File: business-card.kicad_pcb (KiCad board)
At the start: 2 copper layers, 0 parts

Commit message: Placed the CH logo in schematic and pcb
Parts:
- added LOGO1: CH_Logo, business-card:CH_Logo_20mm_SilkScreen, F.Cu at (198.5, 120.7)
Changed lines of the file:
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@@
 		)
+	)
+	(footprint "business-card:CH_Logo_20mm_SilkScreen"
+		(layer "F.Cu")
+		(at 198.5 120.741935)
+		(descr "CH monogram from ch-logo-option-01.svg; 20 mm artwork width, 15.483871 mm height; filled front silkscreen")
+		(tags "CH monogram logo silkscreen")
+		(property "Reference" "LOGO1"
+			(at 0 -9.241935 0)
+			(layer "F.SilkS")
+			(hide yes)
+			(effects
+				(font
+					(size 1 1)
+					(thickness 0.15)
+				)
+			)
+		)
+		(property "Value" "CH_Logo"
+			(at 0 9.241935 0)
+			(layer "F.Fab")
+			(hide yes)
+			(effects
+				(font
+					(size 1 1)
+					(thickness 0.15)
+				)
+			)
+		)
+		(property "Datasheet" ""
+			(at 0 0 0)
+			(layer "F.Fab")
+			(hide yes)
+			(effects
+				(font
+					(size 1.27 1.27)
+				)
+			)
+		)
+		(property "Description" "CH monogram with a 20 mm wide front-silkscreen footprint; no electrical pins"
+			(at 0 0 0)
+			(layer "F.Fab")
+			(hide yes)
+			(effects
+				(font
+					(size 1.27 1.27)
+				)
+			)
+		)
+		(property ki_fp_filters "CH_Logo_*_SilkScreen")
+		(sheetname "/")
+		(sheetfile "business-card.kicad_sch")
+		(units
+			(unit
+				(name "A")
+				(pins)
+			)
+		)
+		(attr exclude_from_pos_files exclude_from_bom allow_missing_courtyard)
+		(duplicate_pad_numbers_are_jumpers no)
+		(fp_poly
+			(pts
+				(xy 0.799439 -7.741935) (xy 0.827489 -7.73913) (xy 0.85554 -7.730715) (xy 0.88359 -7.71669) (xy 0.911641 -7.697055)
+				(xy 3.520337 -5.587658) (xy 3.544881 -5.562412) (xy 3.562412 -5.534362) (xy 3.572931 -5.503506)
+				(xy 3.576438 -5.469846) (xy 3.576438 -0.897616) (xy 7.279102 -0.897616) (xy 7.279102 -4.670407)
+				(xy 7.28068 -4.698852) (xy 7.285414 -4.721073) (xy 7.293303 -4.73707) (xy 7.304348 -4.746844) (xy 7.318548 -4.750394)
+				(xy 7.335905 -4.747721) (xy 7.356417 -4.738824) (xy 7.380084 -4.723703) (xy 9.943899 -2.86115) (xy 9.968443 -2.838359)
+				(xy 9.985975 -2.812062) (xy 9.996494 -2.782258) (xy 10 -2.748948) (xy 10 5.441795) (xy 9.996494 5.475105)
+				(xy 9.985975 5.504909) (xy 9.968443 5.531206) (xy 9.943899 5.553997) (xy 7.380084 7.495091) (xy 7.356417 7.51087)
+				(xy 7.335905 7.520337) (xy 7.318548 7.523492) (xy 7.304348 7.520337) (xy 7.293303 7.51087) (xy 7.285414 7.495091)
+				(xy 7.28068 7.473001) (xy 7.279102 7.4446) (xy 7.279102 1.12202) (xy 3.576438 1.12202) (xy 3.576438 5.497896)
+				(xy 3.572931 5.531381) (xy 3.562412 5.561711) (xy 3.544881 5.588885) (xy 3.520337 5.612903) (xy 0.841515 7.69425)
+				(xy 0.822833 7.708089) (xy 0.805356 7.719451) (xy 0.789084 7.728338) (xy 0.774018 7.734748) (xy 0.760157 7.738681)
+				(xy 0.747502 7.740138) (xy 0.736051 7.739119) (xy 0.725806 7.735624) (xy 0.716767 7.729652) (xy 0.708932 7.721204)
+				(xy 0.702303 7.71028) (xy 0.696879 7.696879) (xy 0.692661 7.681002) (xy 0.689648 7.662649) (xy 0.68784 7.641819)
+				(xy 0.687237 7.618513) (xy 0.687237 -7.629734) (xy 0.68899 -7.656031) (xy 0.69425 -7.678822) (xy 0.703015 -7.698107)
+				(xy 0.715288 -7.713885) (xy 0.731066 -7.726157) (xy 0.750351 -7.734923) (xy 0.773142 -7.740182)
+				(xy 0.799439 -7.741935)
+			)
+			(stroke
+				(width 0)
+				(type solid)
+			)
+			(fill yes)
+			(layer "F.SilkS")
+		)
+		(fp_poly
+			(pts
+				(xy -4.656381 -7.741935) (xy -0.771388 -7.741935) (xy -0.751665 -7.740621) (xy -0.734572 -7.736676)
+				(xy -0.720109 -7.730102) (xy -0.708275 -7.720898) (xy -0.699071 -7.709064) (xy -0.692496 -7.6946)
+				(xy -0.688552 -7.677507) (xy -0.687237 -7.657784) (xy -0.687237 -6.690042) (xy -0.688157 -6.672993)
+				(xy -0.690919 -6.656907) (xy -0.695521 -6.641786) (xy -0.701964 -6.62763) (xy -0.710247 -6.614437)
+				(xy -0.720372 -6.602209) (xy -0.732337 -6.590945) (xy -0.746143 -6.580645) (xy -7.023843 -2.31136)
+				(xy -7.037649 -2.301061) (xy -7.049614 -2.289797) (xy -7.059739 -2.277568) (xy -7.068022 -2.264376)
+				(xy -7.074465 -2.250219) (xy -7.079067 -2.235098) (xy -7.081829 -2.219013) (xy -7.082749 -2.201964)
+				(xy -7.082749 2.356241) (xy -7.081829 2.373291) (xy -7.079067 2.389376) (xy -7.074465 2.404497)
+				(xy -7.068022 2.418654) (xy -7.059739 2.431846) (xy -7.049614 2.444074) (xy -7.037649 2.455338)
+				(xy -7.023843 2.465638) (xy -0.746143 6.720898) (xy -0.732337 6.731197) (xy -0.720372 6.742461)
+				(xy -0.710247 6.75469) (xy -0.701964 6.767882) (xy -0.695521 6.782039) (xy -0.690919 6.79716) (xy -0.688157 6.813245)
+				(xy -0.687237 6.830295) (xy -0.687237 7.657784) (xy -0.688552 7.677507) (xy -0.692496 7.6946) (xy -0.699071 7.709064)
+				(xy -0.708275 7.720898) (xy -0.720109 7.730102) (xy -0.734572 7.736676) (xy -0.751665 7.740621)
+				(xy -0.771388 7.741935) (xy -4.57223 7.741935) (xy -4.606417 7.739481) (xy -4.63885 7.732118) (xy -4.66953 7.719846)
+				(xy -4.698457 7.702665) (xy -9.941094 3.98317) (xy -9.9549 3.972212) (xy -9.966865 3.960379) (xy -9.97699 3.947668)
+				(xy -9.985273 3.934081) (xy -9.991716 3.919618) (xy -9.996318 3.904278) (xy -9.99908 3.888061) (xy -10 3.870968)
+				(xy -10 -3.604488) (xy -9.996494 -3.637798) (xy -9.985975 -3.667602) (xy -9.968443 -3.693899) (xy -9.943899 -3.71669)
+				(xy -4.782609 -7.69986) (xy -4.753682 -7.718268) (xy -4.723001 -7.731417) (xy -4.690568 -7.739306)
+				(xy -4.656381 -7.741935)
+			)
+			(stroke
+				(width 0)
+				(type solid)
+			)
+			(fill yes)
+			(layer "F.SilkS")
+		)
+		(embedded_fonts no)
 	)
 	(embedded_fonts no)

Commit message: Add credit card board outline and getting started components
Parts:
- added BT1: 3V, Battery:BatteryHolder_Keystone_1058_1x2032, B.Cu at (128.5, 88.5)
- added D1: red, LED_THT:LED_D5.0mm, F.Cu at (143.0, 111.0)
- added R1: 1k, Resistor_THT:R_Axial_DIN0309_L9.0mm_D3.2mm_P12.70mm_Horizontal, F.Cu at (114.0, 98.5)
- moved LOGO1 29.3 mm to (170.5, 112.0)
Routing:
- net /led: track 0.00 -> 26.5 mm
- net GND: track 0.00 -> 22.8 mm, vias 0 -> 1
- net VCC: track 0.00 -> 10.8 mm, vias 0 -> 1
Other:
- board outline added: 85.6 x 54 mm

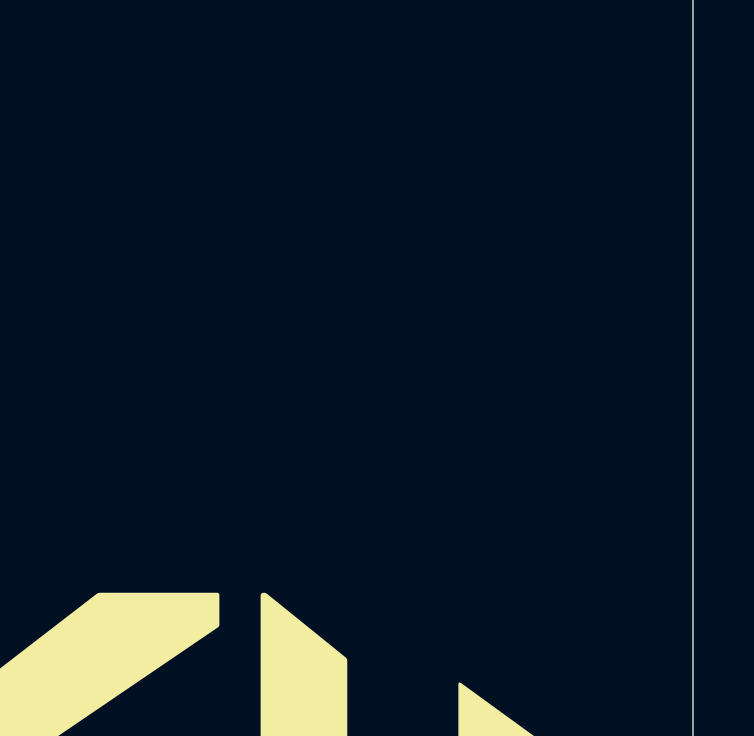
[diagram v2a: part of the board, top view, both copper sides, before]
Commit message: Place the contactless tap icon
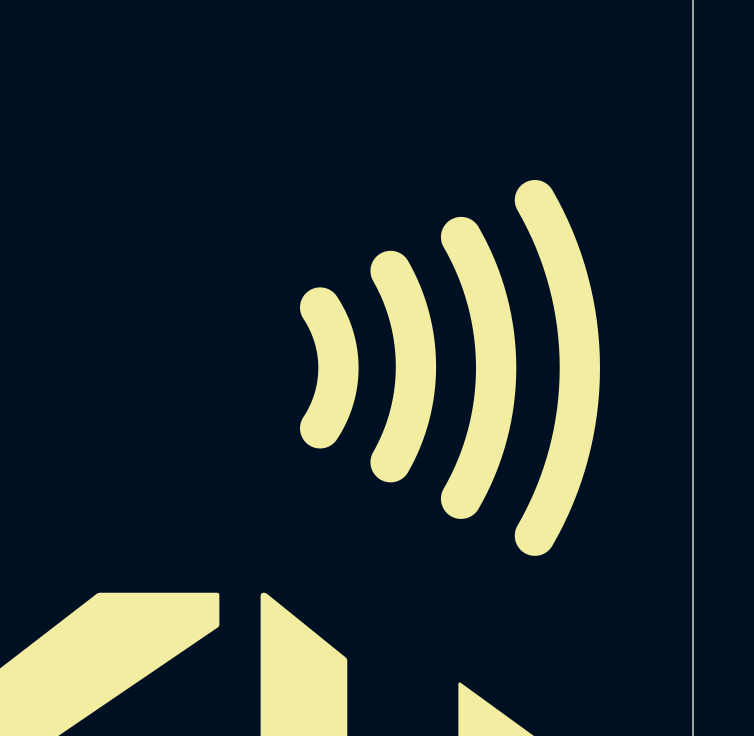
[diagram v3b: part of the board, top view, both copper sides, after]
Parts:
- added LOGO2: Contactless_Logo, business-card:Contactless_Logo_10mm_SilkScreen, F.Cu at (177.5, 96.8)

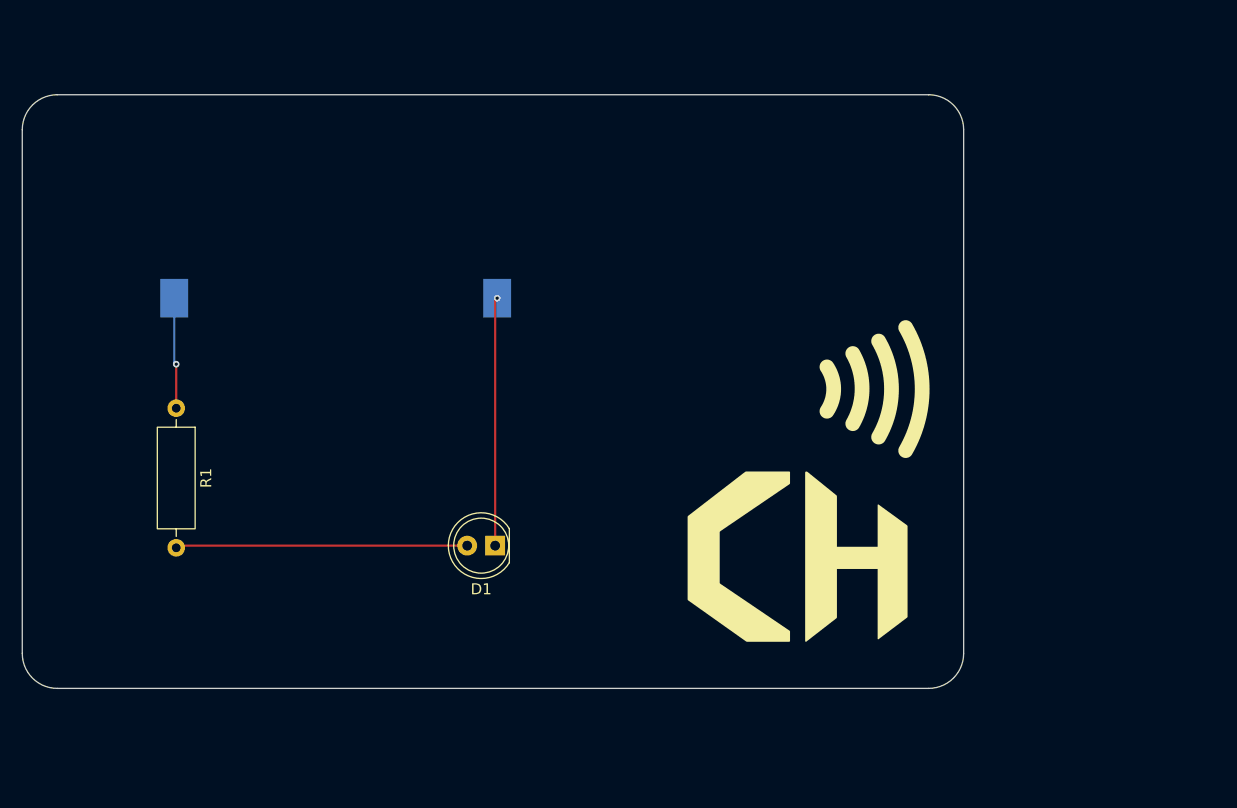
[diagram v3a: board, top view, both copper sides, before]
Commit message: First workable version and extra art
* Most components are in the right place and the PCB is routed
* Tag-connect is still enabled and placed/routed
* Board/schematic is customized for CH, but contact info is example data
* Lots of extra symbols and footprints containing alternative art
* Many alternative components
* A few PCB DRC errors remain to be resolved
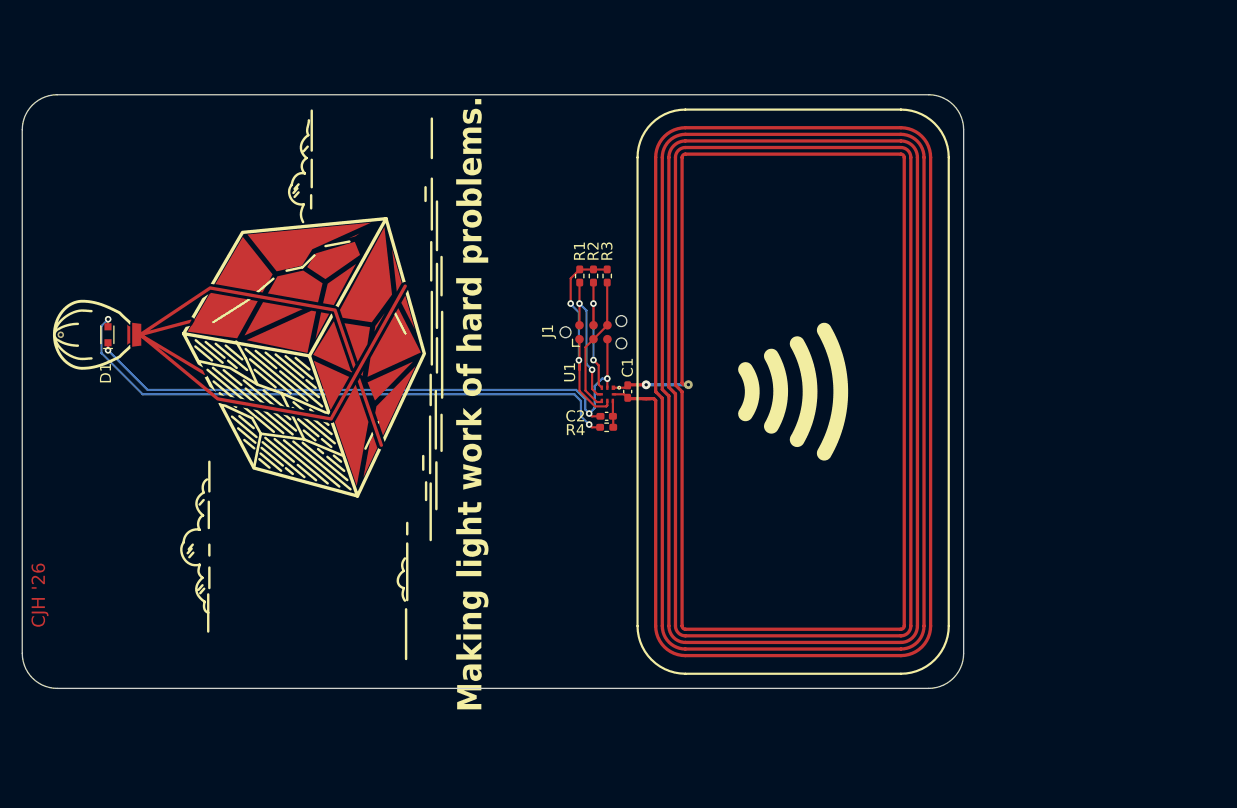
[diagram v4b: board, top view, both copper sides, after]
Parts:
- removed BT1: 3V, Battery:BatteryHolder_Keystone_1058_1x2032
- removed LOGO2: Contactless_Logo, business-card:Contactless_Logo_10mm_SilkScreen
- added ART1: LanternLift_GiftWrap, business-card:LanternLift_GiftWrap_Copper_SilkScreen, F.Cu at (107.6, 91.8)
- added C1: 1.5pF, Capacitor_SMD:C_0402_1005Metric_Pad0.74x0.62mm_HandSolder, F.Cu at (155.1, 97.0)
- added C2: 150nF, Capacitor_SMD:C_0402_1005Metric_Pad0.74x0.62mm_HandSolder, F.Cu at (153.1, 99.2)
- added INFO1: Contact_Info, business-card:Contact_Info_SilkScreen, B.Cu at (180.6, 80.6)
- added J1: TC2030, Connector:Tag-Connect_TC2030-IDC-NL_2x03_P1.27mm_Vertical, F.Cu at (151.9, 91.6)
- added L1: Loboat_NFC_Antenna, business-card:Loboat_NFC_Antenna_48x25mm_5Turns, F.Cu at (170.1, 97.0)
- added R2: 2.2k, Resistor_SMD:R_0402_1005Metric_Pad0.72x0.64mm_HandSolder, F.Cu at (151.9, 86.5)
- added R3: 2.2k, Resistor_SMD:R_0402_1005Metric_Pad0.72x0.64mm_HandSolder, F.Cu at (153.2, 86.5)
- added R4: 330, Resistor_SMD:R_0402_1005Metric_Pad0.72x0.64mm_HandSolder, F.Cu at (153.1, 100.2)
- added SIGN1: CJH_Signature, business-card:CJH_Signature_Copper_Masked, F.Cu at (101.5, 115.5)
- added U1: NT3H2111W0FHKH, business-card:NXP_SOT902-3_XQFN-8_1.6x1.6mm, F.Cu at (153.2, 97.2)
- D1: value red -> A-SP192SS1C-C01-3C; footprint LED_THT:LED_D5.0mm -> business-card:Amicc_A-SP192SS1C-C01-3C_SideView
- LOGO1: moved to B.Cu
- R1: value 1k -> 10k; footprint Resistor_THT:R_Axial_DIN0309_L9.0mm_D3.2mm_P12.70mm_Horizontal -> Resistor_SMD:R_0402_1005Metric_Pad0.72x0.64mm_HandSolder
- moved LOGO1 66.1 mm to (112.5, 80.2), turned to 180 degrees
- moved D1 40.3 mm to (107.6, 91.8), turned to 90 degrees
- moved R1 38.6 mm to (150.7, 86.5)
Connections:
- D1 pad 1: GND -> /led
- D1 pad 2: /led -> GND
- R1 pad 2: /led -> /~{FD}
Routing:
- net GND: track 22.8 -> 57.3 mm, vias 1 -> 3
- net /led: track 26.5 -> 53.0 mm, vias 0 -> 2
- net /~{FD}: track 0.00 -> 13.4 mm, vias 0 -> 2
- net /SDA: track 0.00 -> 12.6 mm
- net /SCL: track 0.00 -> 11.8 mm, vias 0 -> 2
- net VCC: track 10.8 -> 20.5 mm, vias 1 -> 2
- net /LA: track 0.00 -> 6.93 mm, vias 0 -> 1
- net /LB: track 0.00 -> 3.12 mm
- net VBUS: track 0.00 -> 2.42 mm

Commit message: Change cjh signature and CH logo default footprint
This change snagged some other library changes, too, but functionally
it only makes those two changes.
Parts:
- LOGO1: footprint business-card:CH_Logo_20mm_SilkScreen -> business-card:CH_Logo_20mm_Copper
